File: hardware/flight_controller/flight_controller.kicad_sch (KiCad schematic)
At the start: 2 parts, among them U1 Teensy3.6

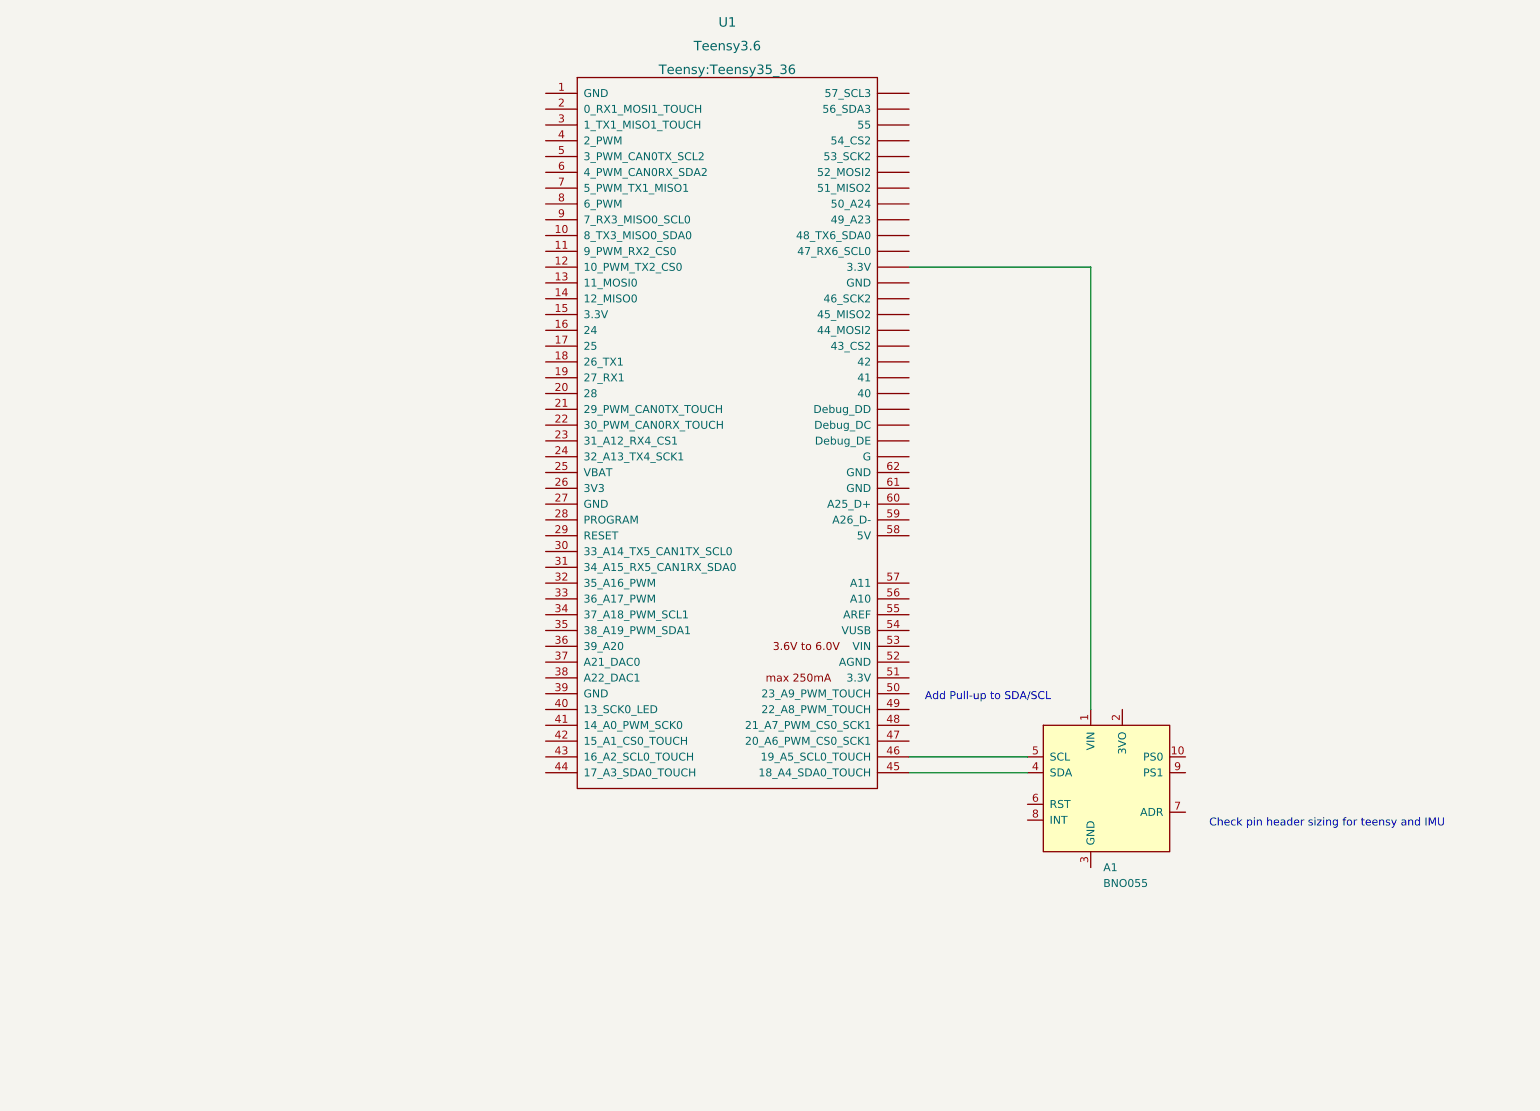
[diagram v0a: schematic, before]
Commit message: PCB design for flight controller is basically complete. Need to verify and have fun with the design before ordering
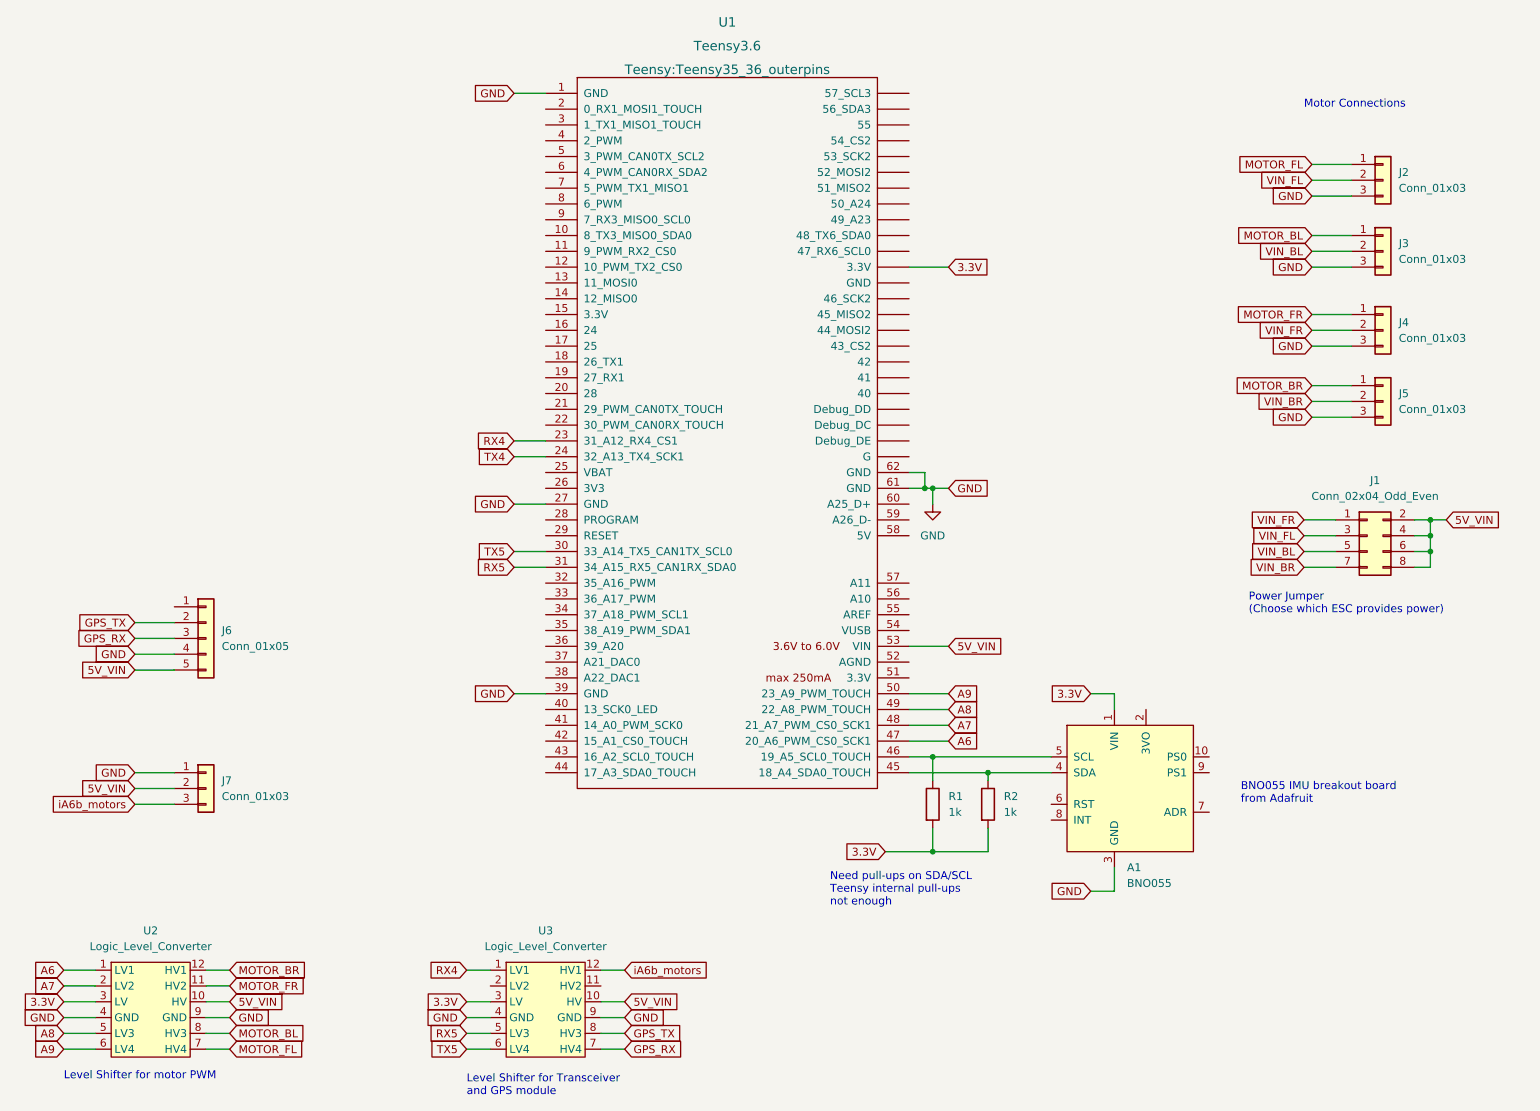
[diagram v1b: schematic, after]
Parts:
- added J1: Conn_02x04_Odd_Even, Connector_PinHeader_2.54mm:PinHeader_2x04_P2.54mm_Vertical, symbol Connector_Generic:Conn_02x04_Odd_Even
- added J2, J3, J4, J5: Conn_01x03, Connector_PinHeader_2.54mm:PinHeader_1x03_P2.54mm_Vertical, symbol Connector_Generic:Conn_01x03
- added J6: Conn_01x05, Connector_PinSocket_2.54mm:PinSocket_1x05_P2.54mm_Vertical, symbol Connector_Generic:Conn_01x05
- added J7: Conn_01x03, Connector_PinSocket_2.54mm:PinSocket_1x03_P2.54mm_Vertical, symbol Connector_Generic:Conn_01x03
- added R1, R2: 1k, Resistor_THT:R_Axial_DIN0207_L6.3mm_D2.5mm_P15.24mm_Horizontal, symbol Device:R
- added U2, U3: Logic_Level_Converter, KleiCad:Logic_Level_Converter, symbol KleiCad:Logic_Level_Converter
- U1: footprint Teensy:Teensy35_36 -> Teensy:Teensy35_36_outerpins
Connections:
- net 3.3V: now reaches A1.1 (VIN), U1.~ (GND)
- net 3.3V: now also R1.2, R2.2, U2.3 (LV), U3.3 (LV)
- net GND: now reaches A1.3 (GND)
- net GND: now also U1.1 (GND), U1.27 (GND), U1.39 (GND), U1.61 (GND), U1.62 (GND), J2.3 (Pin_3), J3.3 (Pin_3), J4.3 (Pin_3), J5.3 (Pin_3), J6.4 (Pin_4), J7.1 (Pin_1), U2.4 (GND), U2.9 (GND), U3.4 (GND), U3.9 (GND)
- net at A1.4 (SDA), U1.45 (18_A4_SDA0_TOUCH): now also R2.1
- net at A1.5 (SCL), U1.46 (19_A5_SCL0_TOUCH): now also R1.1
- net RX4: now reaches U1.23 (31_A12_RX4_CS1)
- net RX4: now also U3.1 (LV1)
- net TX4: now reaches U1.24 (32_A13_TX4_SCK1)
- net TX5: now reaches U1.30 (33_A14_TX5_CAN1TX_SCL0)
- net TX5: now also U3.6 (LV4)
- net RX5: now reaches U1.31 (34_A15_RX5_CAN1RX_SDA0)
- net RX5: now also U3.5 (LV3)
- net A6: now reaches U1.47 (20_A6_PWM_CS0_SCK1)
- net A6: now also U2.1 (LV1)
- net A7: now reaches U1.48 (21_A7_PWM_CS0_SCK1)
- net A7: now also U2.2 (LV2)
- net A8: now reaches U1.49 (22_A8_PWM_TOUCH)
- net A8: now also U2.5 (LV3)
- net A9: now reaches U1.50 (23_A9_PWM_TOUCH)
- net A9: now also U2.6 (LV4)
- net 5V_VIN: now reaches U1.53 (VIN)
- net 5V_VIN: now also J1.2 (Pin_2), J1.4 (Pin_4), J1.6 (Pin_6), J1.8 (Pin_8), J6.5 (Pin_5), J7.2 (Pin_2), U2.10 (HV), U3.10 (HV)
- new net GPS_RX: J6.3 (Pin_3), U3.7 (HV4)
- new net GPS_TX: J6.2 (Pin_2), U3.8 (HV3)
- new net MOTOR_BL: J3.1 (Pin_1), U2.8 (HV3)
- new net MOTOR_BR: J5.1 (Pin_1), U2.12 (HV1)
- new net MOTOR_FL: J2.1 (Pin_1), U2.7 (HV4)
- new net MOTOR_FR: J4.1 (Pin_1), U2.11 (HV2)
- new net VIN_BL: J1.5 (Pin_5), J3.2 (Pin_2)
- new net VIN_BR: J1.7 (Pin_7), J5.2 (Pin_2)
- new net VIN_FL: J1.3 (Pin_3), J2.2 (Pin_2)
- new net VIN_FR: J1.1 (Pin_1), J4.2 (Pin_2)
- new net iA6b_motors: J7.3 (Pin_3), U3.12 (HV1)
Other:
- note added: "BNO055 IMU breakout board from Adafruit"
- note added: "Level Shifter for Transceiver and GPS module"
- note added: "Level Shifter for motor PWM"
- note added: "Motor Connections"
- note added: "Need pull-ups on SDA/SCL Teensy internal pull-ups not enough"
- note added: "Power Jumper (Choose which ESC provides power)"
- note removed: "Add Pull-up to SDA/SCL"
- note removed: "Check pin header sizing for teensy and IMU"
- moved on the sheet: A1
